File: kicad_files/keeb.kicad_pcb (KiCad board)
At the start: 2 copper layers, 369.3 x 148.8 mm, 231 parts, among them SW10 SW_Push, SW11 SW_Push, SW12 SW_Push, SW13 SW_Push, SW14 SW_Push, SW15 SW_Push, SW16 SW_Push, SW17 SW_Push, SW18 SW_Push, SW19 SW_Push, SW2 RotaryEncoder_Switch, SW20 SW_Push, SW21 SW_Push, SW22 SW_Push, SW23 SW_Push, SW24 SW_Push, SW25 SW_Push, SW26 SW_Push, SW27 SW_Push, SW28 SW_Push, SW29 SW_Push, SW3 SW_Push, SW30 SW_Push, SW31 SW_Push, SW32 SW_Push, SW33 SW_Push, SW34 SW_Push, SW35 SW_Push, SW36 SW_Push, SW37 SW_Push, SW38 SW_Push, SW39 SW_Push, SW4 SW_Push, SW40 SW_Push, SW41 SW_Push, SW42 SW_Push, SW43 SW_Push, SW44 SW_Push, SW45 SW_Push, SW46 SW_Push, SW47 SW_Push, SW48 SW_Push, SW49 SW_Push, SW5 SW_Push, SW50 SW_Push, SW51 SW_Push, SW52 SW_Push, SW53 SW_Push, SW54 SW_Push, SW55 SW_Push, SW56 SW_Push, SW6 SW_Push, SW7 SW_Push, SW8 SW_Push, SW9 SW_Push, U2 ER_OLEDM0.91_1x-I2C

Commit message: Flipped two diodes that were on the wrong side
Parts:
- D1, D42: moved to B.Cu
- moved D50 46.5 mm to (380.5, 59.3), turned to 120 degrees
- moved C21 46.5 mm to (37.2, 154.3), turned to 90 degrees
- moved D38 45.6 mm to (371.0, 42.8), turned to 120 degrees
- moved C15 45.5 mm to (37.2, 135.2), turned to 90 degrees
- moved D14 45.4 mm to (352.0, 9.90), turned to 120 degrees
- moved D59 45.4 mm to (42.0, 155.4), turned to 180 degrees
- moved D26 45.2 mm to (361.5, 26.4), turned to 120 degrees
- moved C3 45.1 mm to (37.2, 96.8), turned to 90 degrees
- moved C9 45.0 mm to (37.2, 116.2), turned to 90 degrees
- moved SW39 45.0 mm to (42.3, 150.7), turned to 0 degrees
- moved D58 44.3 mm to (42.0, 136.4), turned to 180 degrees
- moved D109 44.1 mm to (372.9, 66.2), turned to -150 degrees
- moved SW27 44.0 mm to (42.3, 131.6), turned to 0 degrees
- moved SW50 43.9 mm to (370.9, 62.3), turned to 30 degrees
- moved SW3 43.9 mm to (42.3, 93.5), turned to 0 degrees
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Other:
- board size 369.3 x 148.8 mm -> 356.8 x 199.7 mm

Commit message: changed ec11 footprint
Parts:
- SW2: footprint Rotary_Encoder:RotaryEncoder_Alps_EC11E-Switch_Vertical_H20mm -> PCM_marbastlib-various:ROT_Alps_EC11E-Switch
- moved D50 46.5 mm to (387.7, 105.3), turned to 105 degrees
- moved C21 46.5 mm to (31.5, 108.1), turned to 75 degrees
- moved D38 45.6 mm to (382.8, 86.9), turned to 105 degrees
- moved C15 45.5 mm to (36.4, 89.7), turned to 75 degrees
- moved D14 45.4 mm to (372.9, 50.2), turned to 105 degrees
- moved D59 45.4 mm to (35.8, 110.5), turned to 165 degrees
- moved D26 45.2 mm to (377.8, 68.5), turned to 105 degrees
- moved C3 45.1 mm to (46.4, 52.6), turned to 75 degrees
- moved C9 45.0 mm to (41.3, 71.3), turned to 75 degrees
- moved SW39 45.0 mm to (37.3, 106.0), turned to -15 degrees
- moved D58 44.3 mm to (40.7, 92.1), turned to 165 degrees
- moved D109 44.1 mm to (378.6, 110.0), turned to -165 degrees
- moved SW27 44.0 mm to (42.2, 87.6), turned to -15 degrees
- moved SW50 43.9 mm to (377.6, 105.6), turned to 15 degrees
- moved SW3 43.9 mm to (52.1, 50.8), turned to -15 degrees
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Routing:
- net /ROT_B: track 52.9 -> 49.6 mm
- net Net-(D1-~-Pad2): track 13.1 -> 9.92 mm
- net /ROT_A: track 31.1 -> 30.3 mm, vias 0 -> 2
- net /COL_4: track 250.4 -> 249.7 mm
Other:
- board size 356.8 x 199.7 mm -> 369.3 x 148.8 mm

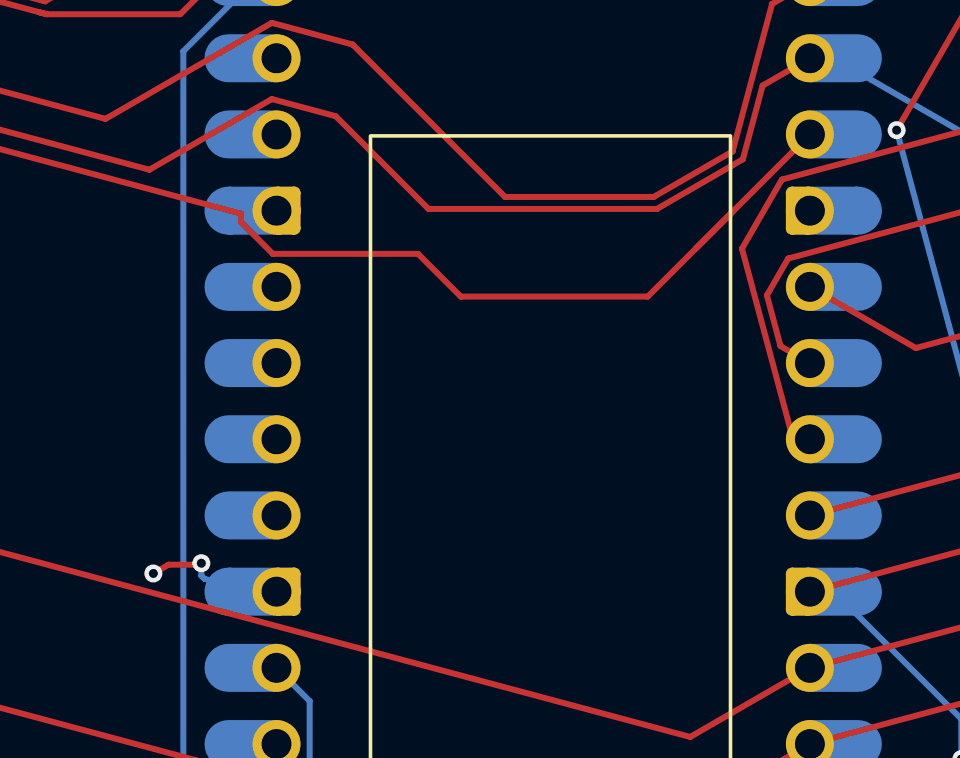
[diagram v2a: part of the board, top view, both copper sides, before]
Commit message: Started on the 3d model
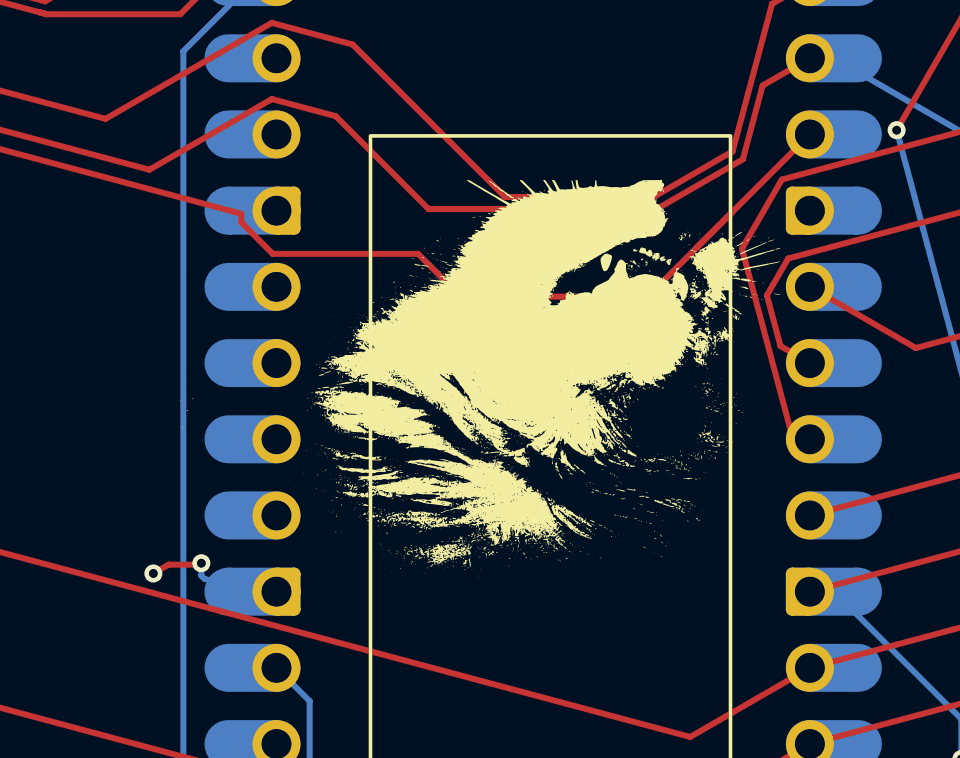
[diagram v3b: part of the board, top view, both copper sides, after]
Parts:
- added G***: LOGO, LOGO, F.Cu at (204.8, 85.7)
